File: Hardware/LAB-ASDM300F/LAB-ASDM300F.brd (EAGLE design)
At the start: 18.4 x 10.8 mm, 20 parts, among them J1 SULLINSSMTHEADER-4, J2 SULLINSSMTHEADER-4, U1 TPS62240DRVTG4, U2 MIC94325, U3 MAX4377HAUA

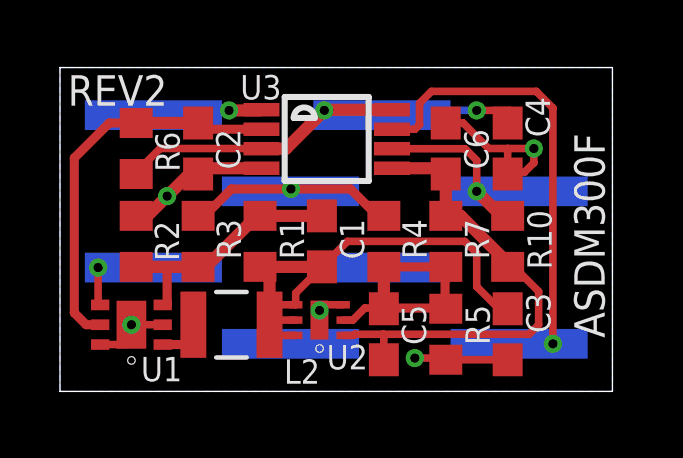
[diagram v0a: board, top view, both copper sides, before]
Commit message: 1) Moved the LDO up and to the left a few mils. 2) Changed from three pads output from the inductor to the LDO to just one. *) Both of these changes provide a bit of thermal relief such that when the solder is being reflowed that the inductor wont want to slide towards the LDO. Also, this eliminated bends in BUCKOUT and LDOADJ circuits.
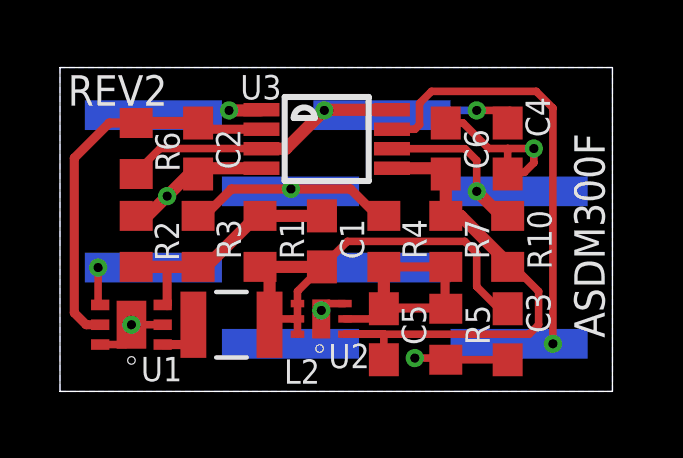
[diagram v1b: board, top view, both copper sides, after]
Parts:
- moved U2 0.07 mm to (8.71, 2.42)
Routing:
- net N$4: track 16.2 -> 17.4 mm
- net BUCKOUT: track 17.8 -> 17.1 mm
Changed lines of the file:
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@@
 <attribute name="VALUE" x="13.0175" y="8.73125" size="1.27" layer="27" rot="R270"/>
 </element>
-<element name="U2" library="My Library-adm" package="SON65P160X160X80-7N" value="MIC94325" x="8.651875" y="2.38125" smashed="yes" rot="R180">
-<attribute name="NAME" x="8.8884125" y="0.73421875" size="0.8128" layer="25" font="vector" ratio="10" rot="SR0"/>
-<attribute name="VALUE" x="12.106275" y="6.19125" size="2.0828" layer="27" ratio="10" rot="SR180"/>
+<element name="U2" library="My Library-adm" package="SON65P160X160X80-7N" value="MIC94325" x="8.71140625" y="2.4209375" smashed="yes" rot="R180">
+<attribute name="NAME" x="8.94794375" y="0.77390625" size="0.8128" layer="25" font="vector" ratio="10" rot="SR0"/>
+<attribute name="VALUE" x="12.16580625" y="6.2309375" size="2.0828" layer="27" ratio="10" rot="SR180"/>
 </element>
 <element name="R7" library="rcl" package="R0603" value="130k" x="12.85875" y="5.000625" smashed="yes" rot="R90">
@@
 <wire x1="2.834375" y1="5.77125" x2="3.571875" y2="6.50875" width="0.4064" layer="1"/>
 <wire x1="4.309375" y1="7.24625" x2="3.571875" y2="6.50875" width="0.4064" layer="1"/>
-<via x="8.651875" y="2.69875" extent="1-16" drill="0.3048"/>
-<wire x1="9.439275" y1="2.88765" x2="8.840775" y2="2.88765" width="0.254" layer="1"/>
+<via x="8.71140625" y="2.69875" extent="1-16" drill="0.3048"/>
 <wire x1="12.85875" y1="8.94625" x2="12.85875" y2="9.04875" width="0.254" layer="1"/>
-<wire x1="8.651875" y1="2.69875" x2="8.651875" y2="2.38125" width="0.254" layer="1"/>
-<wire x1="8.651875" y1="2.38125" x2="8.647875" y2="2.37725" width="0.254" layer="1"/>
+<wire x1="8.71140625" y1="2.38125" x2="8.70740625" y2="2.4169375" width="0.254" layer="1"/>
 <contactref element="C2" pad="2"/>
 <contactref element="J1" pad="P$4"/>
@@
 <wire x1="2.1971" y1="1.5621" x2="2.38125" y2="1.74625" width="0.254" layer="1"/>
 <wire x1="2.38125" y1="1.74625" x2="2.38125" y2="2.2225" width="0.254" layer="1"/>
-<wire x1="8.651875" y1="2.69875" x2="8.840775" y2="2.88765" width="0.254" layer="1"/>
 <wire x1="2.54" y1="5.850625" x2="2.619375" y2="5.77125" width="0.254" layer="1"/>
 <wire x1="2.619375" y1="5.77125" x2="2.834375" y2="5.77125" width="0.254" layer="1"/>
@@
 <wire x1="15.478125" y1="7.3025" x2="15.795625" y2="7.62" width="0.254" layer="1"/>
 <wire x1="15.795625" y1="7.62" x2="15.795625" y2="8.09625" width="0.254" layer="1"/>
+<wire x1="9.49880625" y1="2.9273375" x2="8.93999375" y2="2.9273375" width="0.254" layer="1"/>
+<wire x1="8.93999375" y1="2.9273375" x2="8.71140625" y2="2.69875" width="0.254" layer="1"/>
+<wire x1="8.70740625" y1="2.4169375" x2="8.70740625" y2="2.69475" width="0.254" layer="1"/>
+<wire x1="8.70740625" y1="2.69475" x2="8.71140625" y2="2.69875" width="0.254" layer="1"/>
 </signal>
 <signal name="N$1">
@@
 <wire x1="10.771875" y1="1.031875" x2="10.795" y2="1.055" width="0.254" layer="1"/>
 <wire x1="10.8131" y1="1.0731" x2="10.795" y2="1.055" width="0.254" layer="1"/>
-<wire x1="9.82265625" y1="1.905" x2="10.77515625" y2="1.905" width="0.254" layer="1"/>
-<wire x1="10.77515625" y1="1.905" x2="15.636875" y2="1.905" width="0.254" layer="1"/>
-<wire x1="15.636875" y1="1.905" x2="15.954375" y2="2.2225" width="0.254" layer="1"/>
 <wire x1="15.954375" y1="2.2225" x2="15.954375" y2="3.33375" width="0.254" layer="1"/>
 <wire x1="15.954375" y1="3.33375" x2="15.1375" y2="4.150625" width="0.254" layer="1"/>
@@
 <wire x1="13.358125" y1="5.850625" x2="14.9225" y2="4.28625" width="0.4064" layer="1"/>
 <wire x1="14.9225" y1="4.150625" x2="14.9225" y2="4.28625" width="0.4064" layer="1"/>
-<wire x1="9.439275" y1="1.86685" x2="9.78450625" y2="1.86685" width="0.254" layer="1"/>
-<wire x1="9.78450625" y1="1.86685" x2="9.82265625" y2="1.905" width="0.254" layer="1"/>
-<wire x1="10.795" y1="1.055" x2="10.795" y2="1.88515625" width="0.254" layer="1"/>
-<wire x1="10.795" y1="1.88515625" x2="10.77515625" y2="1.905" width="0.254" layer="1"/>
+<wire x1="9.49880625" y1="1.905" x2="9.49880625" y2="1.9065375" width="0.254" layer="1"/>
+<wire x1="9.49880625" y1="1.9065375" x2="15.6384125" y2="1.9065375" width="0.254" layer="1"/>
+<wire x1="15.6384125" y1="1.9065375" x2="15.954375" y2="2.2225" width="0.254" layer="1"/>
+<wire x1="9.49880625" y1="1.9065375" x2="10.7934625" y2="1.9065375" width="0.254" layer="1"/>
+<wire x1="10.7934625" y1="1.9065375" x2="10.795" y2="1.905" width="0.254" layer="1"/>
+<wire x1="10.795" y1="1.905" x2="10.795" y2="1.055" width="0.254" layer="1"/>
 </signal>
 <signal name="LDOADJ">
@@
 <contactref element="R4" pad="2"/>
 <contactref element="C5" pad="2"/>
-<wire x1="9.759125" y1="2.37725" x2="10.16" y2="2.778125" width="0.254" layer="1"/>
-<wire x1="10.16" y1="2.778125" x2="10.771875" y2="2.778125" width="0.254" layer="1"/>
 <wire x1="10.771875" y1="2.778125" x2="10.795" y2="2.755" width="0.254" layer="1"/>
 <wire x1="10.795" y1="2.755" x2="10.795" y2="2.38125" width="0.254" layer="1"/>
 <wire x1="11.089375" y1="2.460625" x2="10.795" y2="2.755" width="0.254" layer="1"/>
-<wire x1="9.439275" y1="2.37725" x2="9.759125" y2="2.37725" width="0.254" layer="1"/>
 <wire x1="10.771875" y1="2.778125" x2="12.835625" y2="2.778125" width="0.3048" layer="1"/>
 <wire x1="12.835625" y1="2.778125" x2="12.85875" y2="2.755" width="0.254" layer="1"/>
@@
 <wire x1="10.795" y1="4.150625" x2="12.85875" y2="4.150625" width="0.3048" layer="1"/>
 <wire x1="10.795" y1="4.150625" x2="10.795" y2="2.8575" width="0.4064" layer="1"/>
+<wire x1="9.49880625" y1="2.4169375" x2="10.4569375" y2="2.4169375" width="0.254" layer="1"/>
+<wire x1="10.4569375" y1="2.4169375" x2="10.795" y2="2.755" width="0.254" layer="1"/>
 </signal>
 <signal name="BUCKOUT">
@@
 <wire x1="6.8564" y1="2.7289" x2="6.82625" y2="2.69875" width="0.254" layer="1"/>
 <wire x1="6.8564" y1="2.7289" x2="6.8564" y2="3.01625" width="0.254" layer="1"/>
-<wire x1="7.856475" y1="2.88765" x2="6.985" y2="2.88765" width="0.254" layer="1"/>
 <wire x1="6.985" y1="2.88765" x2="6.8564" y2="3.01625" width="0.254" layer="1"/>
-<wire x1="7.856475" y1="2.37725" x2="7.13975" y2="2.37725" width="0.254" layer="1"/>
 <wire x1="7.13975" y1="2.37725" x2="6.985" y2="2.2225" width="0.254" layer="1"/>
 <wire x1="7.13975" y1="2.37725" x2="7.13975" y2="2.38525" width="0.254" layer="1"/>
@@
 <wire x1="6.8564" y1="3.88235" x2="6.6675" y2="4.07125" width="0.254" layer="1"/>
 <wire x1="6.6675" y1="4.07125" x2="6.6675" y2="4.150625" width="0.254" layer="1"/>
-<wire x1="7.856475" y1="2.88765" x2="7.856475" y2="3.27585" width="0.254" layer="1"/>
-<wire x1="7.856475" y1="3.27585" x2="8.73125" y2="4.150625" width="0.254" layer="1"/>
-<wire x1="7.856475" y1="1.86685" x2="7.34065" y2="1.86685" width="0.254" layer="1"/>
-<wire x1="7.34065" y1="1.86685" x2="6.985" y2="2.2225" width="0.254" layer="1"/>
 <wire x1="14.9225" y1="2.755" x2="14.628125" y2="2.755" width="0.254" layer="1"/>
 <wire x1="14.628125" y1="2.755" x2="13.890625" y2="3.4925" width="0.254" layer="1"/>
@@
 <wire x1="13.49375" y1="5.000625" x2="9.58125" y2="5.000625" width="0.254" layer="1"/>
 <wire x1="9.58125" y1="5.000625" x2="8.73125" y2="4.150625" width="0.254" layer="1"/>
+<wire x1="7.91600625" y1="2.4169375" x2="7.91600625" y2="2.9273375" width="0.254" layer="1"/>
+<wire x1="7.91600625" y1="2.4169375" x2="7.1794375" y2="2.4169375" width="0.254" layer="1"/>
+<wire x1="7.1794375" y1="2.4169375" x2="6.985" y2="2.2225" width="0.254" layer="1"/>
+<wire x1="7.91600625" y1="1.9065375" x2="7.91600625" y2="2.4169375" width="0.254" layer="1"/>
+<wire x1="7.91600625" y1="2.9273375" x2="7.91600625" y2="3.33538125" width="0.254" layer="1"/>
+<wire x1="7.91600625" y1="3.33538125" x2="8.73125" y2="4.150625" width="0.254" layer="1"/>
 </signal>
 <signal name="VOUT">
